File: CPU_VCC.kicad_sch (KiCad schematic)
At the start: 1 part

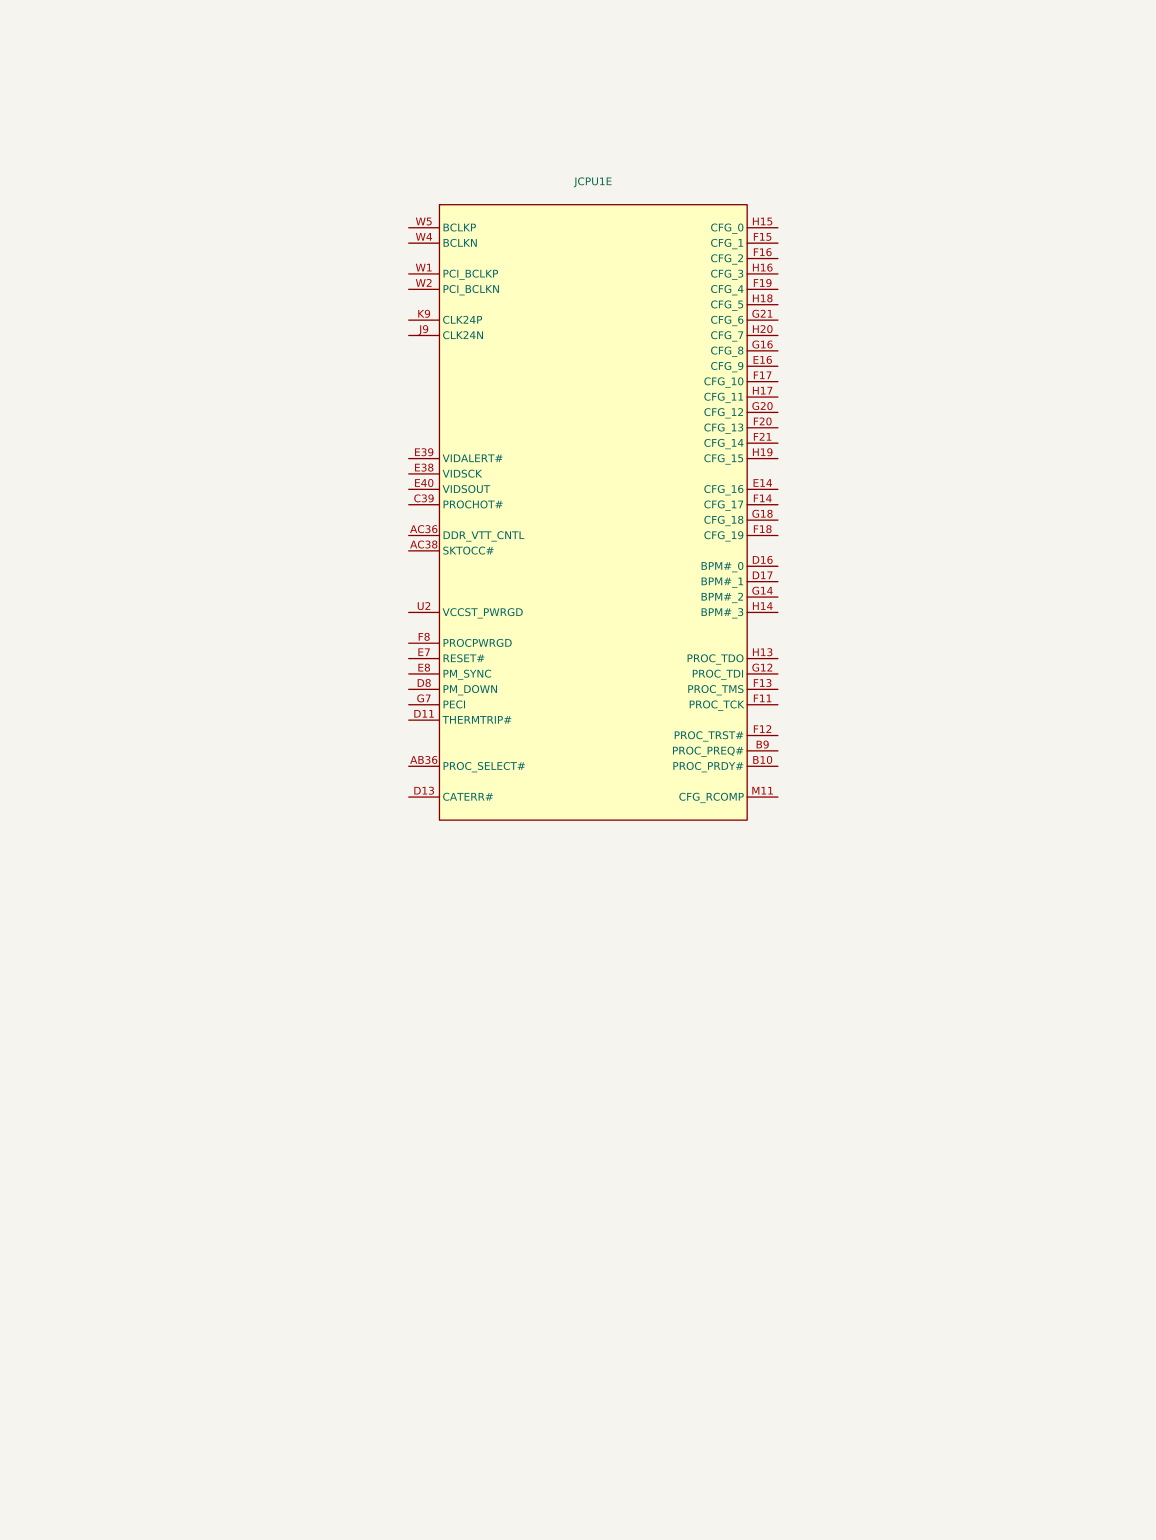
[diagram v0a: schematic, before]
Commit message: Added CPU GND and Core VCC symbols
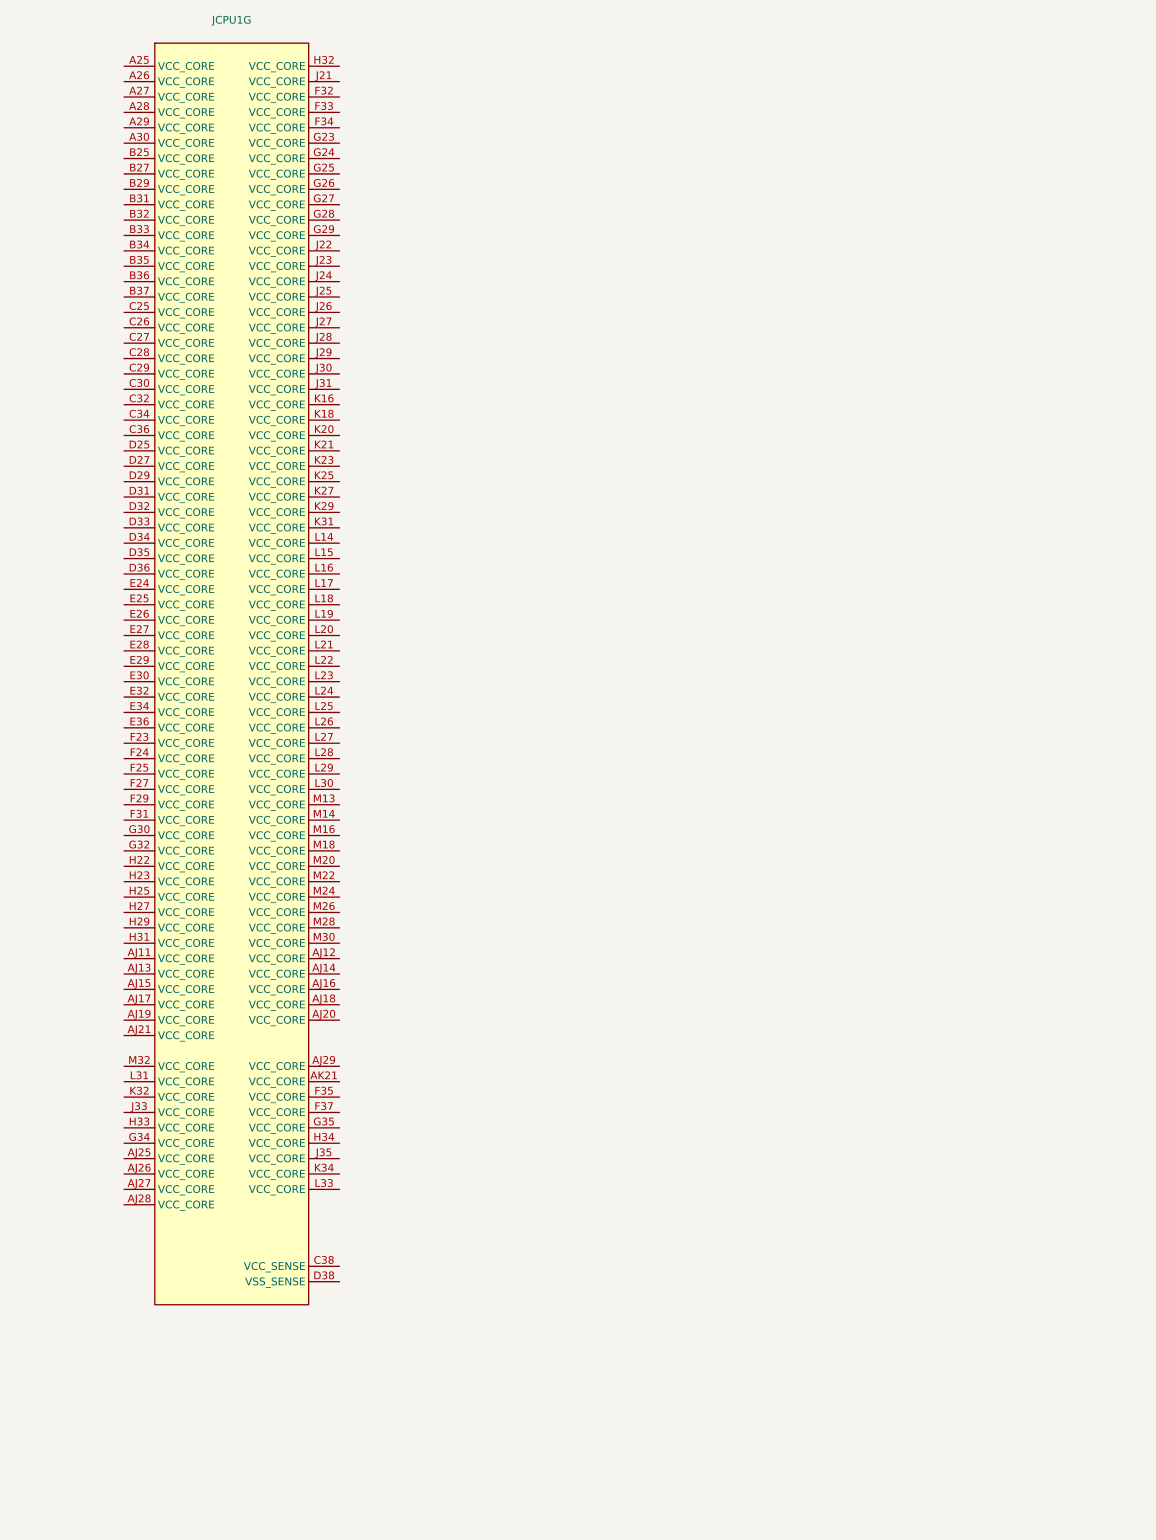
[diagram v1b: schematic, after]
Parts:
- removed JCPU1: ~, A-my-stuff:LGA-1151_L47.1-W42.5-P0.91_PE115127-4041-01H, symbol A-my-stuff:Intel_CFL_1151
- added JCPU1: ~, A-my-stuff:LGA-1151_L47.1-W42.5-P0.91_PE115127-4041-01H, symbol A-my-stuff:Intel_CFL_1151
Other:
- title: CPU Clock, CFG, VID & JTAG -> CPU Power supply

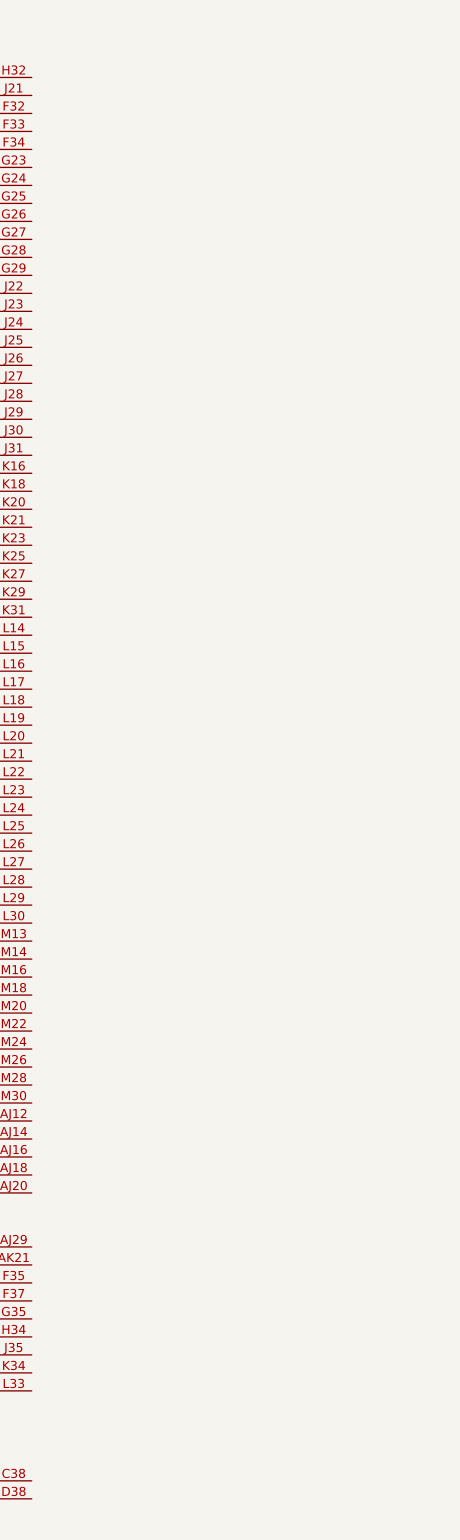
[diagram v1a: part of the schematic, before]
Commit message: Added iGPU VCC symbol
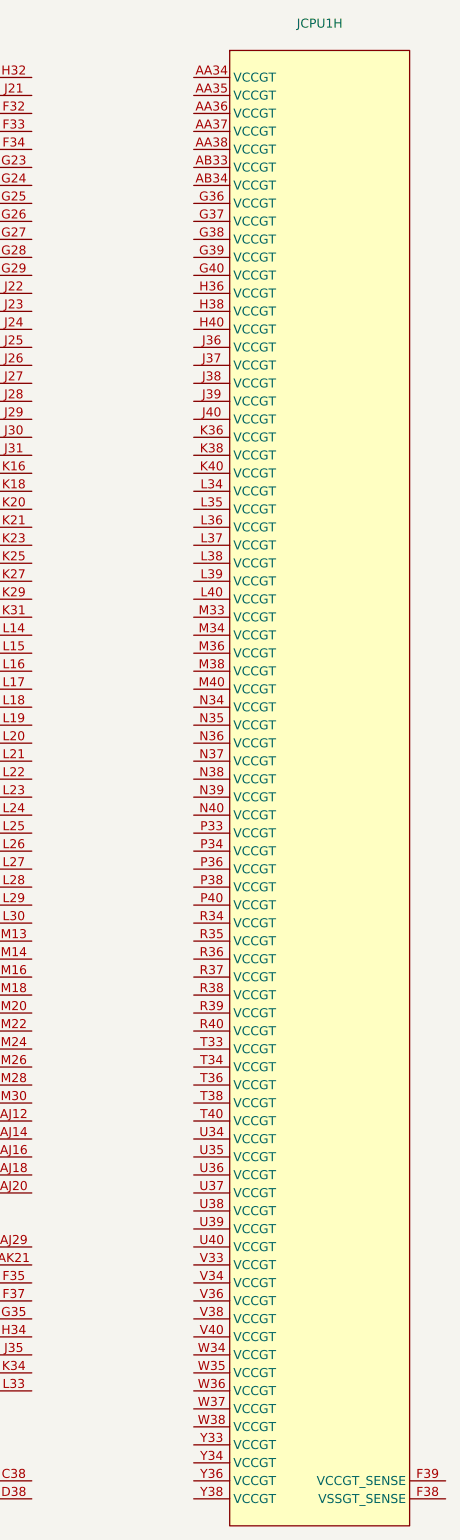
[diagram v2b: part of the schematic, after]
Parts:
- added unit 8 of JCPU1

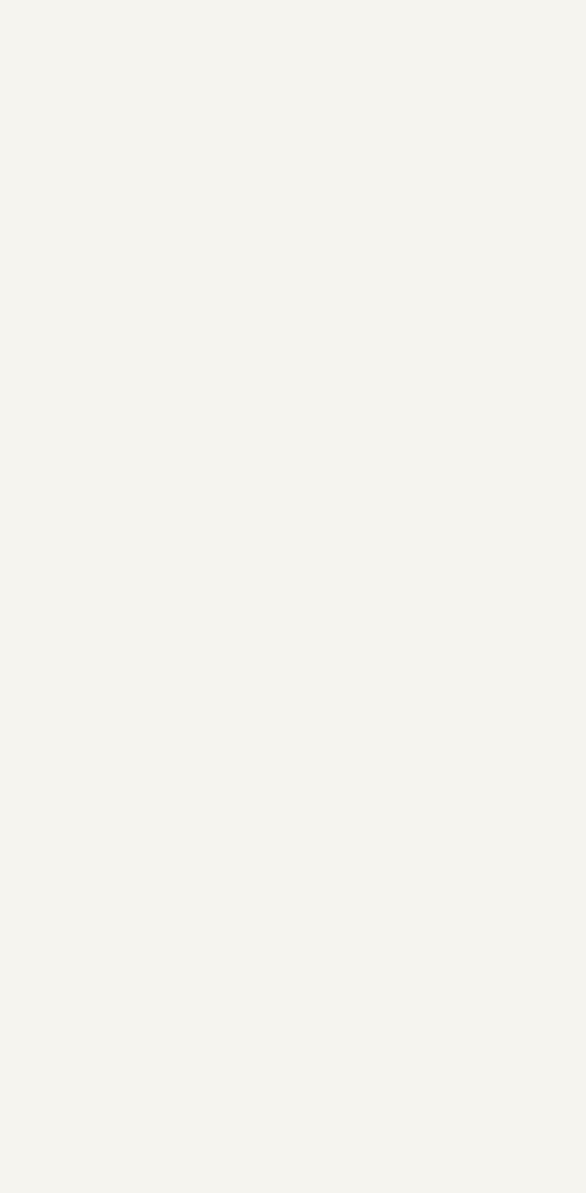
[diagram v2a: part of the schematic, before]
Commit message: Added CPU Misc VCC symbol
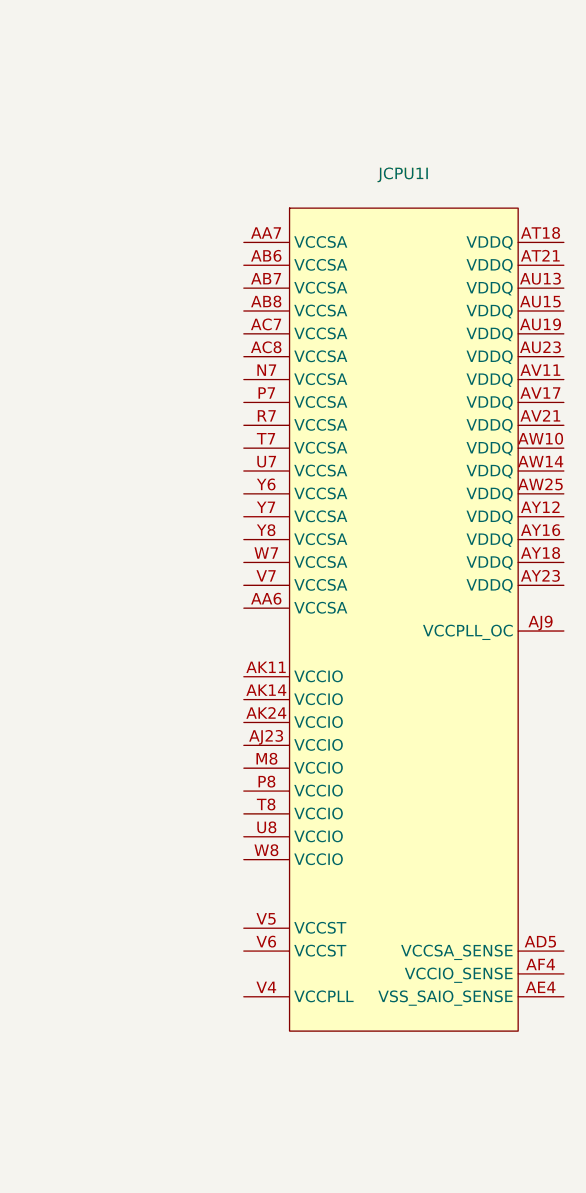
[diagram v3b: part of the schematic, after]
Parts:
- added unit 9 of JCPU1

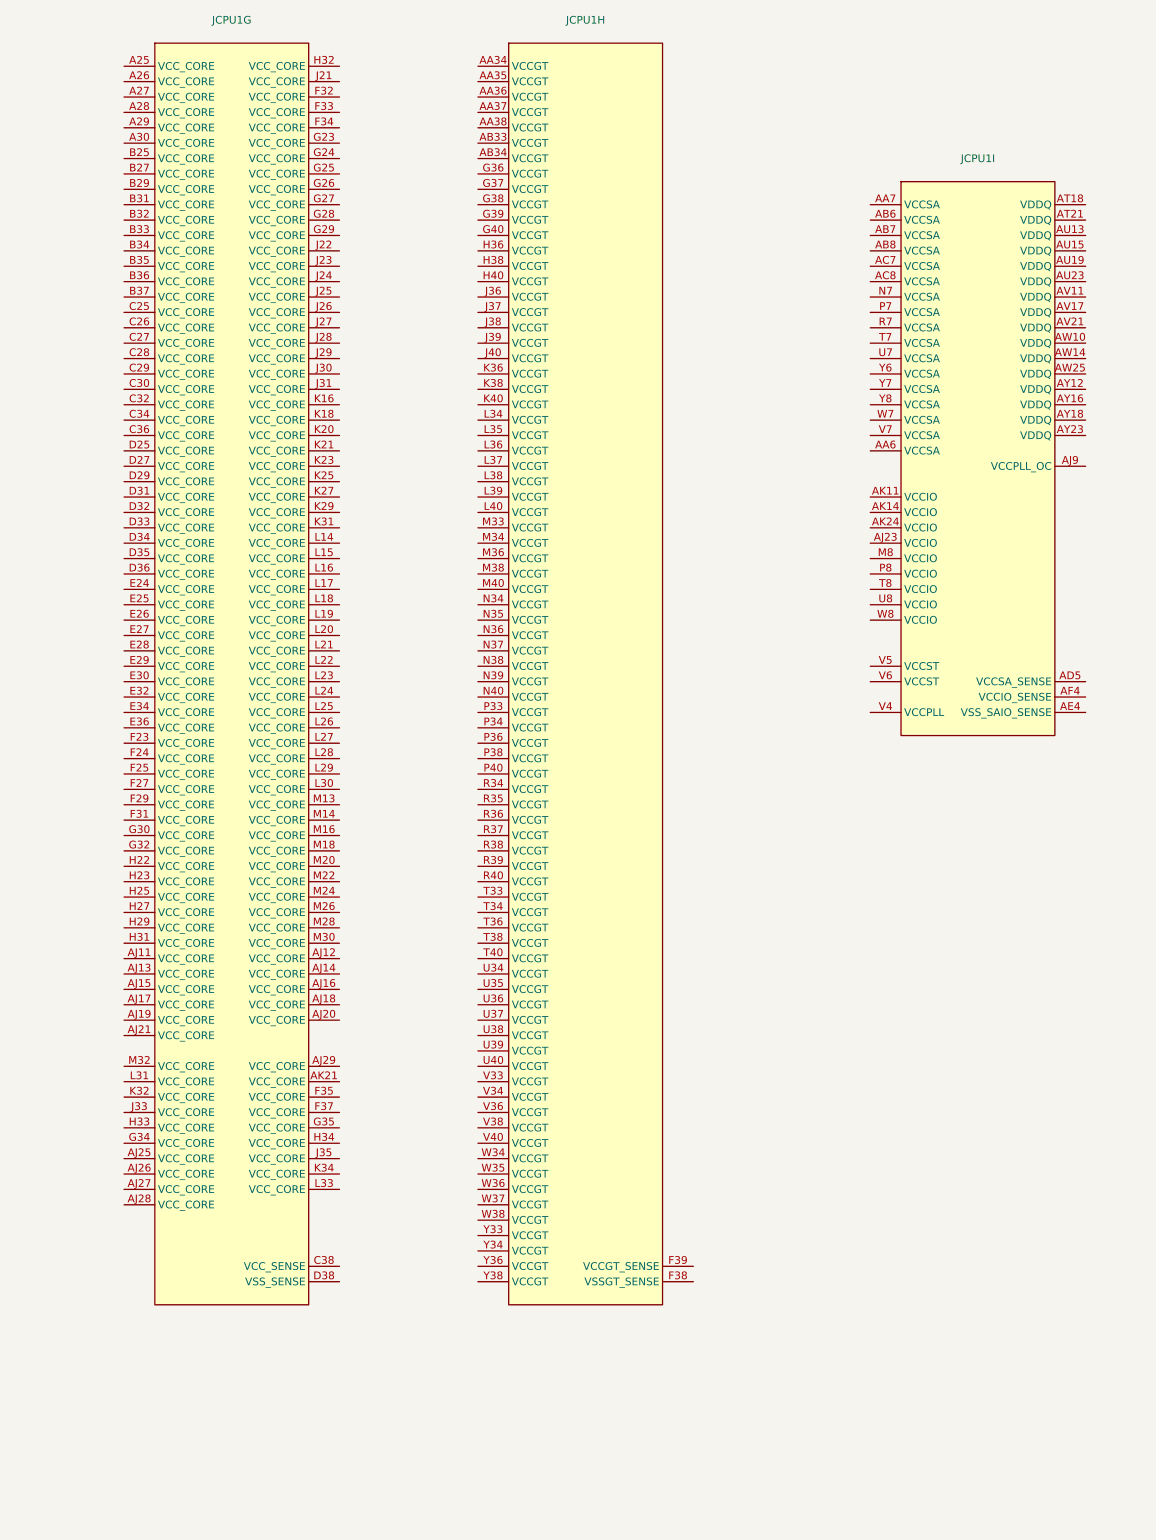
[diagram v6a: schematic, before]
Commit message: Added first PCH symbol and footprint
THANKS @mothenjoyer69 so much for extracting and converting the PCH footprint from a laptop boardview ❤️
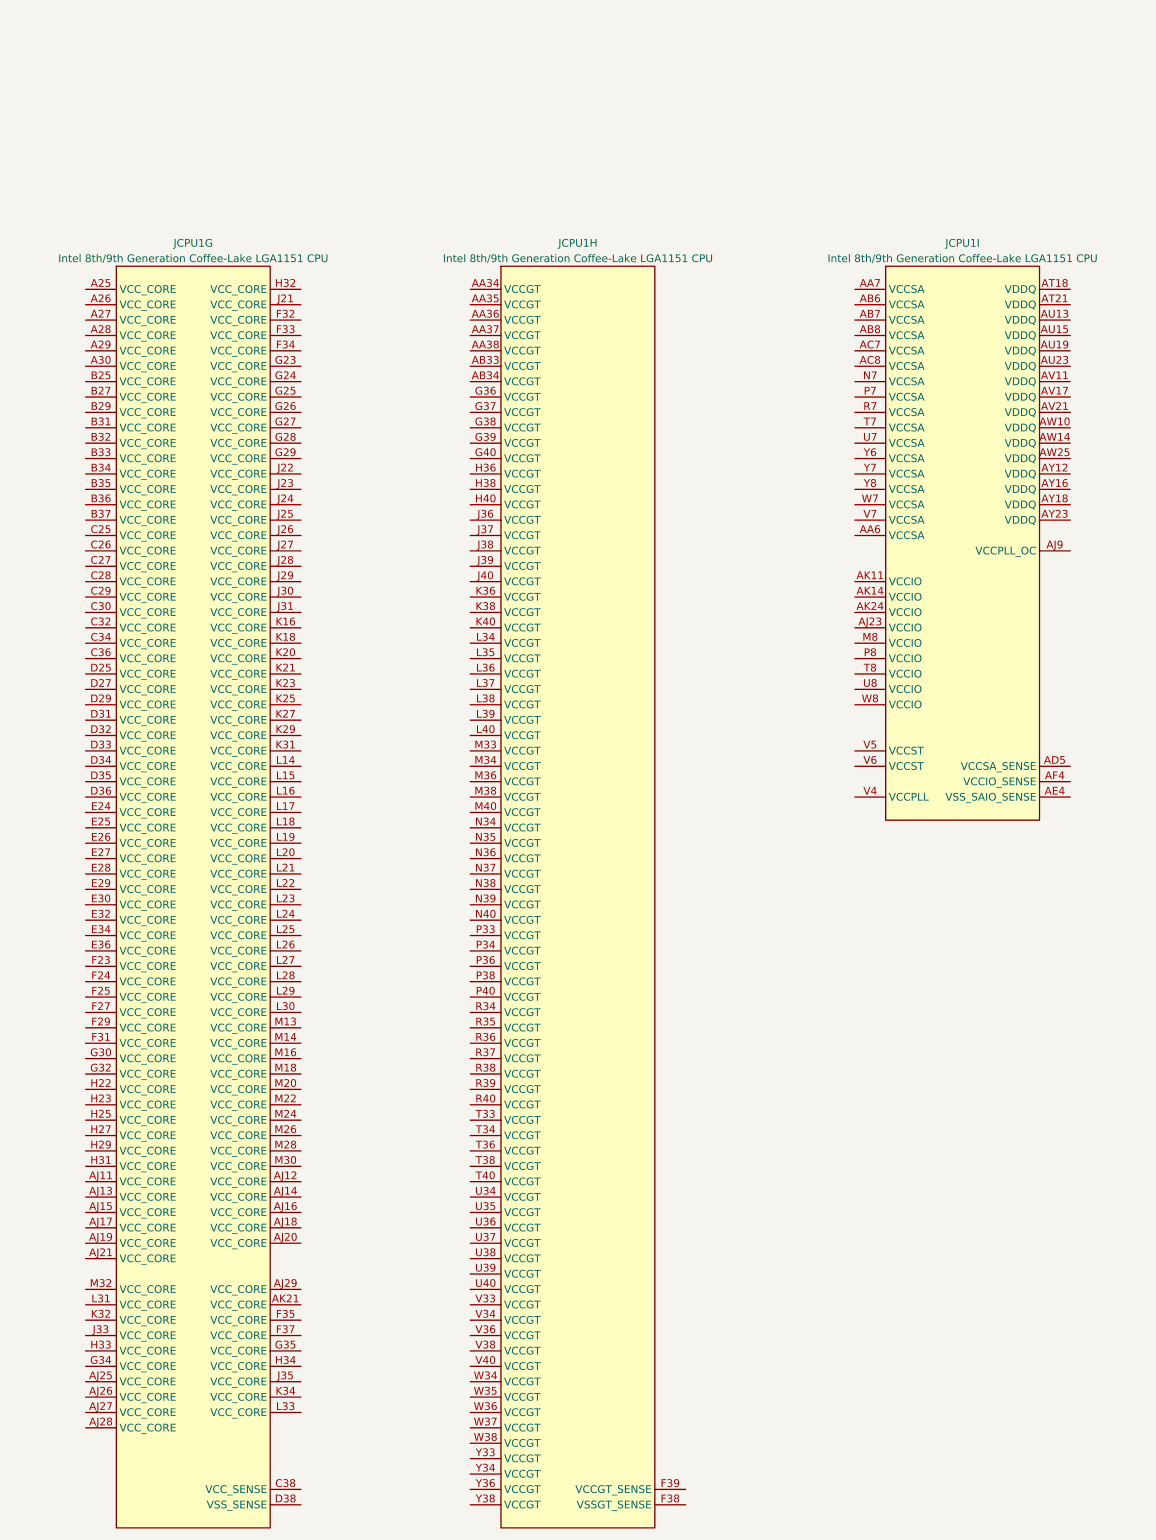
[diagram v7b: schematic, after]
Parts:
- JCPU1: value ~ -> Intel 8th/9th Generation Coffee-Lake LGA1151 CPU
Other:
- moved on the sheet: JCPU1G, JCPU1H, JCPU1I
